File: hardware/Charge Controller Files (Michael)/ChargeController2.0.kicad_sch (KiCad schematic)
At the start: 90 parts, among them J1 GND_TEST_01x01_Pin, J10 SOL_TEST_01x01_Pin, J13 Conn-1x2, J14 Conn-1x2, J15 Conn-1x2, J17 SCL_MAS_01x01_Pin, J18 SDA_MAS_01x01_Pin, J19 SYS-1x2, J2 SP_01x02_Pin, J3 BATT_TEST_01x01_Pin, J4 3.3V_PULLUP_01x02_Pin, J5 BATT_01x02_Pin, J6 Conn-1x2, J7 Conn-1x2, J8 Conn-1x2, J9 SYS_TEST_01x01_Pin, Q1 SI2318DS-T1-E3, Q10 SI2318DS-T1-E3, Q11 SI2318DS-T1-E3, Q12 SI2318DS-T1-E3, Q2 SI2318DS-T1-E3, Q3 SI2318DS-T1-E3, Q4 SI2318DS-T1-E3, Q5 AONS66614, Q6 AONS66614, Q7 AONS66614, Q8 AONS66614, Q9 SI2318DS-T1-E3, SW1 100SP1T1B1M1QEH, U1 BQ25756ERRVR

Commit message: Update ChargeController2.0.kicad_sch
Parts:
- Q5, Q6, Q7, Q8: Arrow Part Number (none) -> AONS66614; Arrow Price/Stock (none) -> https://www.arrow.com/en/products/aons66614/alpha-and-omega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

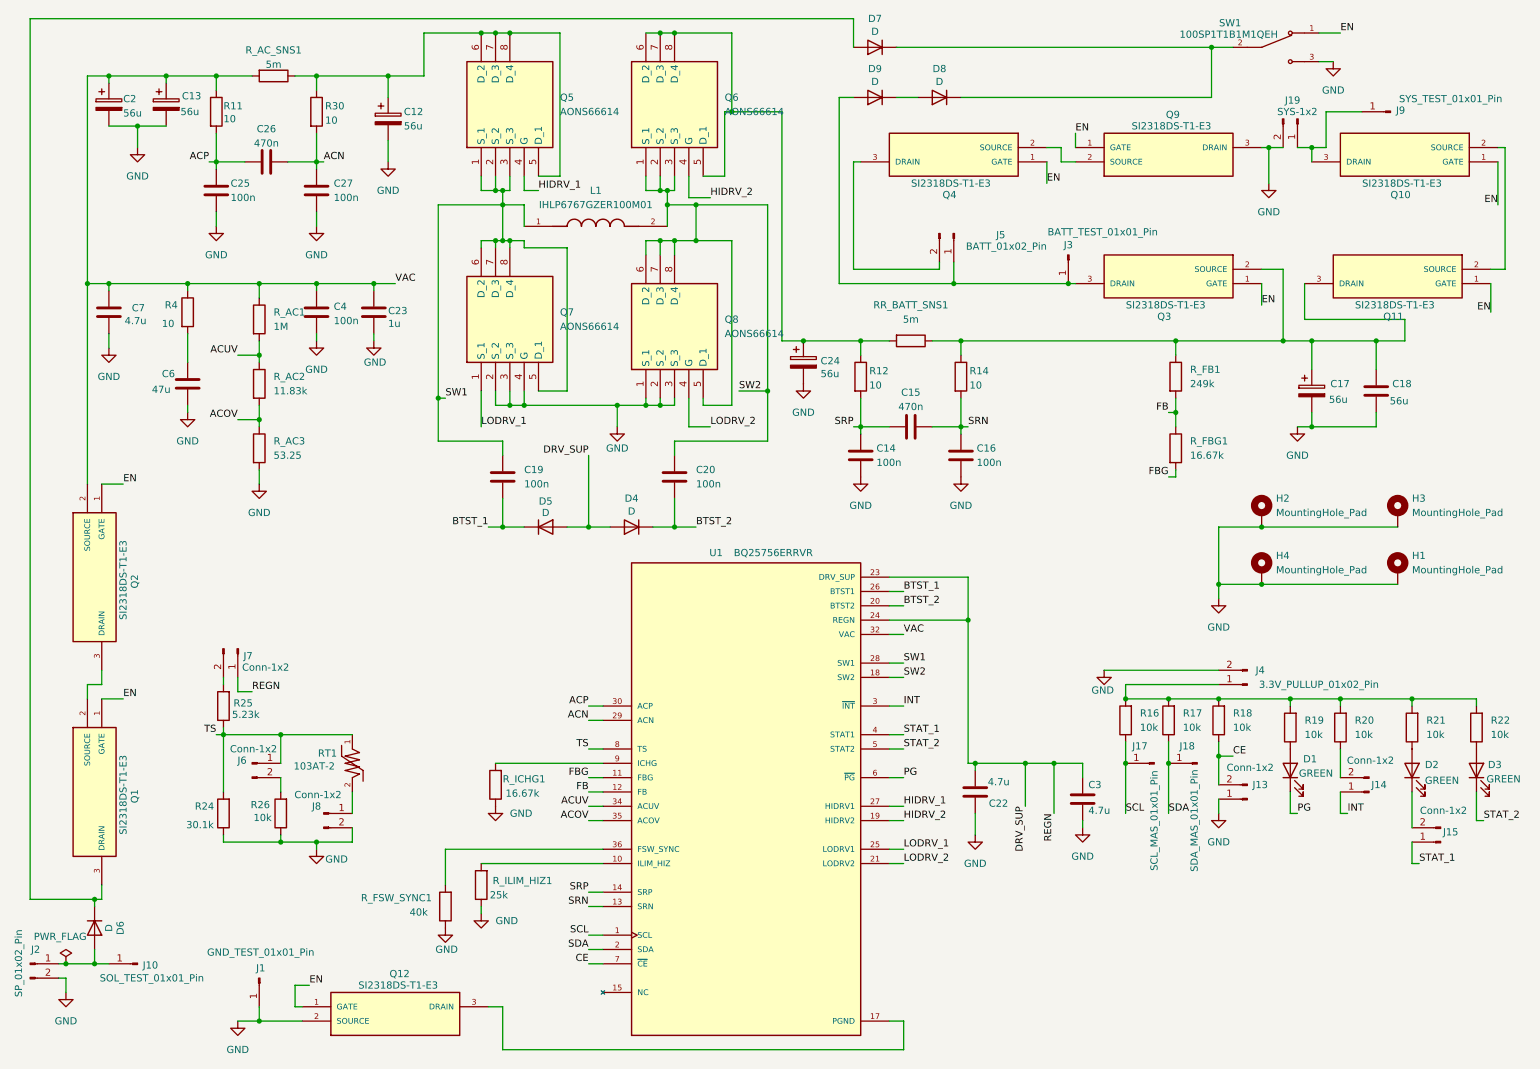
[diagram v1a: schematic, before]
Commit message: updated footprints
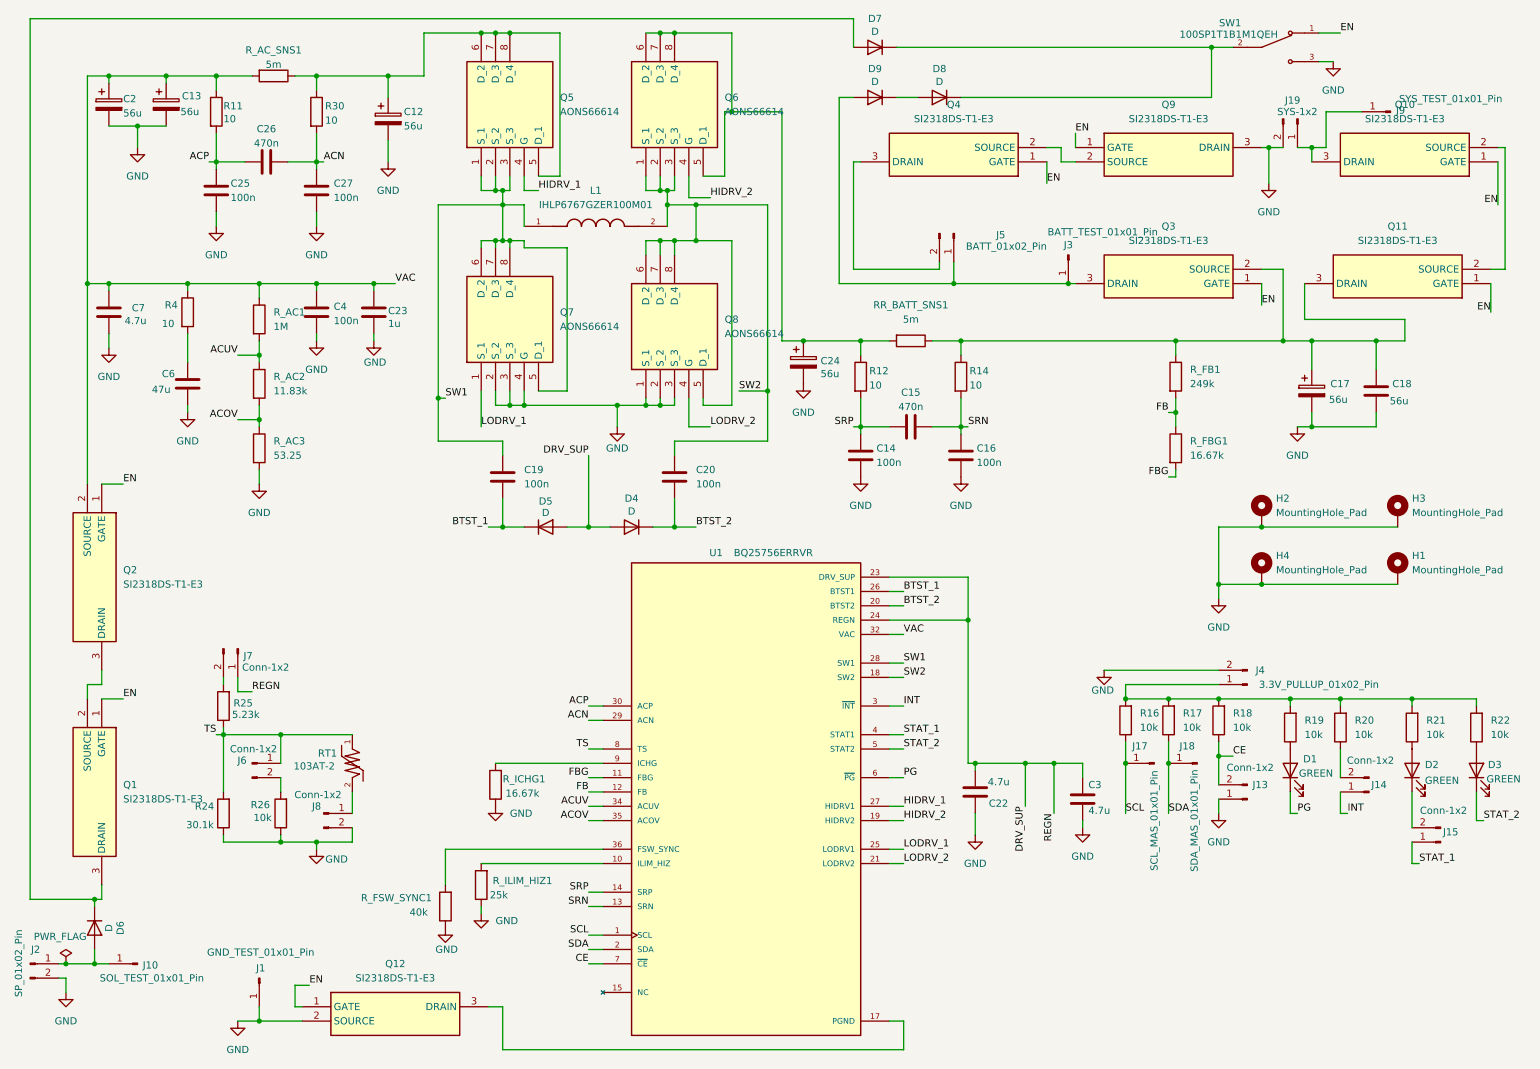
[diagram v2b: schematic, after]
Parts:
- Q1, Q2, Q3, Q4: ARROW_PART_NUMBER SI2318DS-T1-E3 -> (none); ARROW_PRICE-STOCK https://www.arrow.com/en/products/si2318ds-t1-e3/vishay -> (none); Availability In Stock -> (none); Check_prices https://www.snapeda.com/parts/SI2318DS-T1-E3/Vishay/view-pa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 -> (none); DESCRIPTION VISHAY - SI2318DS-T1-E3 - N CHANNEL MOSFET, 40V, 3.9A, TO-2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 -> (none); Description_1 N-CHANNEL 40-V (D-S) MOSFET | Siliconix / Vishay SI2318DS-T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 -> (none); HEIGHT 1.02mm -> (none); Height (none) -> 1.02; MANUFACTURER_NAME Vishay -> (none); MANUFACTURER_PART_NUMBER SI2318DS-T1-E3 -> (none); MF Vishay Siliconix -> (none); MOUSER_PART_NUMBER 781-SI2318DS-E3 -> (none); MOUSER_PRICE-STOCK https://www.mouser.co.uk/ProductDetail/Vishay-Semiconductor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 -> (none); MP SI2318DS-T1-E3 -> (none); Manufacturer_Name (none) -> Vishay; Manufacturer_Part_Number (none) -> SI2318DS-T1-E3; Mouser Part Number (none) -> 781-SI2318DS-E3; Mouser Price/Stock (none) -> https://www.mouser.co.uk/ProductDetail/Vishay-Semiconductor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; Package SOT-23-3 Vishay Siliconix -> (none); Price None -> (none); SnapEDA_Link https://www.snapeda.com/parts/SI2318DS-T1-E3/Vishay/view-pa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 -> (none)
- Q10, Q11, Q12, Q9: footprint bmsfootprints:SI2318DS-T1-E3 -> bmsfootprints:SOT95P237X102-3N; ARROW_PART_NUMBER SI2318DS-T1-E3 -> (none); ARROW_PRICE-STOCK https://www.arrow.com/en/products/si2318ds-t1-e3/vishay -> (none); Availability In Stock -> (none); Check_prices https://www.snapeda.com/parts/SI2318DS-T1-E3/Vishay/view-pa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 -> (none); DESCRIPTION VISHAY - SI2318DS-T1-E3 - N CHANNEL MOSFET, 40V, 3.9A, TO-2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 -> (none); Description_1 N-CHANNEL 40-V (D-S) MOSFET | Siliconix / Vishay SI2318DS-T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 -> (none); HEIGHT 1.02mm -> (none); Height (none) -> 1.02; MANUFACTURER_NAME Vishay -> (none); MANUFACTURER_PART_NUMBER SI2318DS-T1-E3 -> (none); MF Vishay Siliconix -> (none); MOUSER_PART_NUMBER 781-SI2318DS-E3 -> (none); MOUSER_PRICE-STOCK https://www.mouser.co.uk/ProductDetail/Vishay-Semiconductor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 -> (none); MP SI2318DS-T1-E3 -> (none); Manufacturer_Name (none) -> Vishay; Manufacturer_Part_Number (none) -> SI2318DS-T1-E3; Mouser Part Number (none) -> 781-SI2318DS-E3; Mouser Price/Stock (none) -> https://www.mouser.co.uk/ProductDetail/Vishay-Semiconductor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; Package SOT-23-3 Vishay Siliconix -> (none); Price None -> (none); SnapEDA_Link https://www.snapeda.com/parts/SI2318DS-T1-E3/Vishay/view-pa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 -> (none)

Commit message: Diode/Small Fixes
- Changed Inhibits MOSFETs to all be same footprint
- Changing diodes
   - Inhibits/Power Path -> SS24
   - Bootstrap -> BAT54
- LODRV_1 pin incorrectly placed
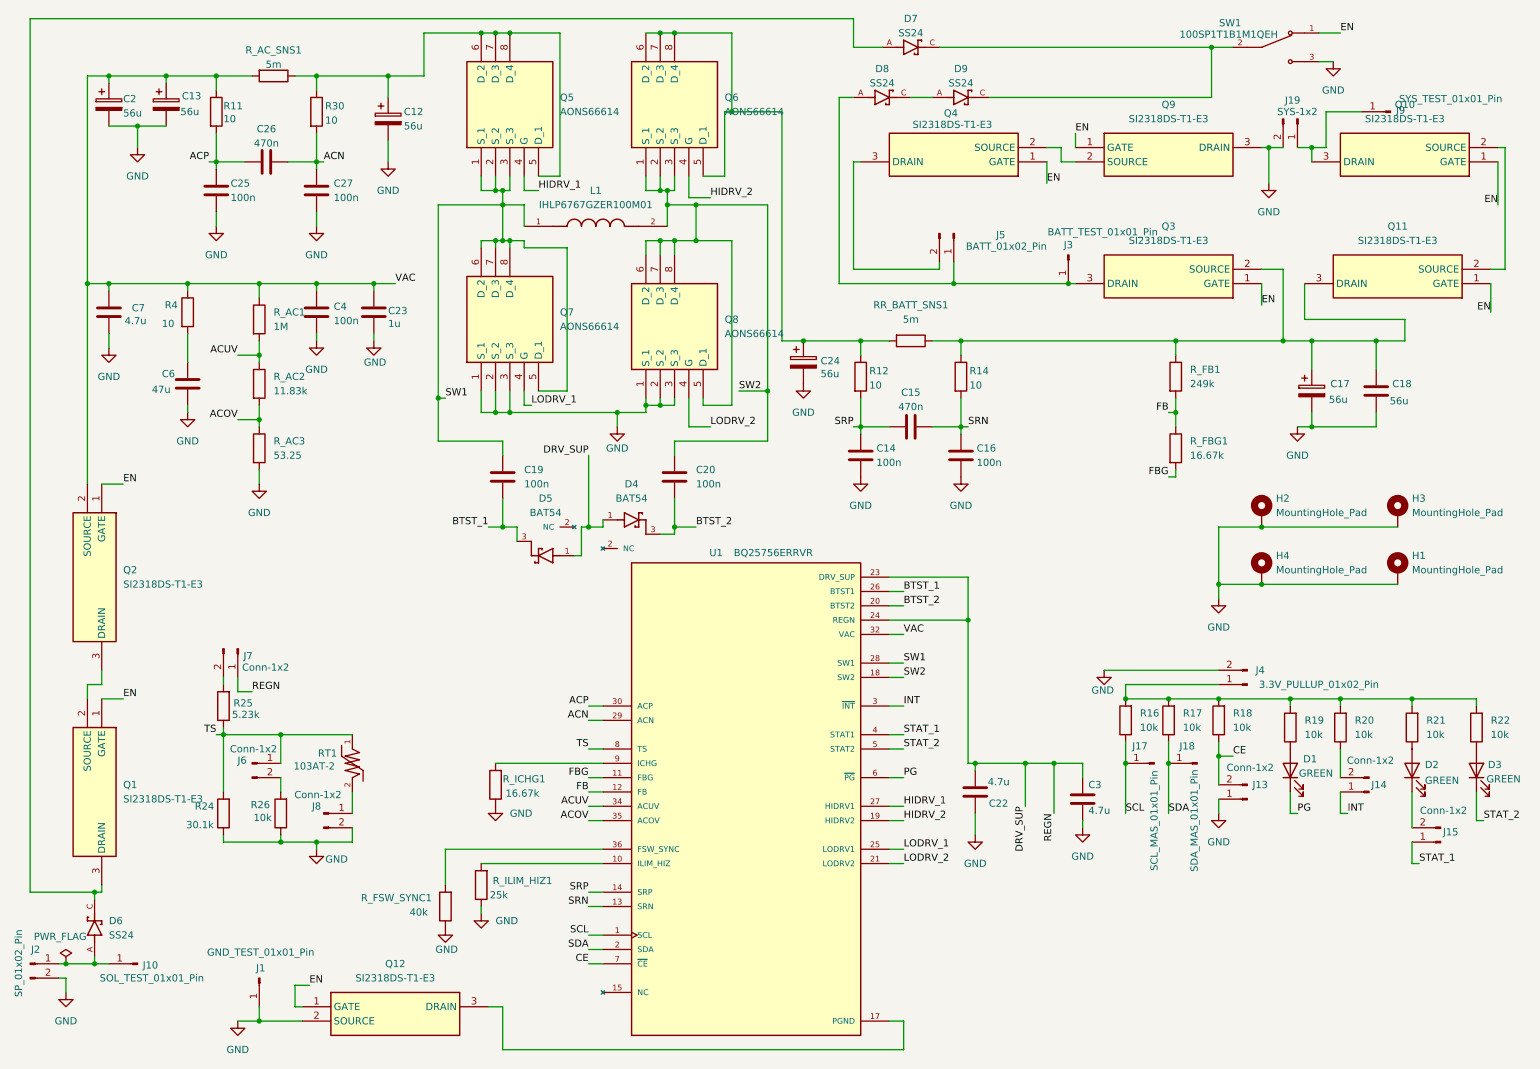
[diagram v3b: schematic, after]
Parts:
- removed D4, D5, D6, D7, D8, D9: D, bmsfootprints:DO-214AC, symbol Device:D
- added D4, D5: BAT54, bmsfootprints:BAT54, symbol BAT54:BAT54
- added D6, D7, D8, D9: SS24, bmsfootprints:SS24, symbol SS24:SS24
- J5: footprint Connector_PinHeader_2.54mm:PinHeader_1x01_P2.54mm_Vertical -> Connector_PinHeader_2.54mm:PinHeader_1x02_P2.54mm_Vertical
- Q10, Q11, Q12, Q9: footprint bmsfootprints:SOT95P237X102-3N -> bmsfootprints:SI2318DS-T1-E3
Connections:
- net BTST_1: now also D5.3
- net BTST_2: now also D4.3
- net DRV_SUP: now also D4.1, D5.1
- net GND: now also Q7.1 (S_1); no longer Q7.4 (G)
- net LODRV_1: now also Q7.4 (G); no longer Q7.1 (S_1)
- net at J3.1 (Pin_1), J5.1 (Pin_1), Q3.3 (DRAIN): now also D8.A
- net at SW1.2: now also D7.C, D9.C
- net at Q1.3 (DRAIN): now also D6.C, D7.A
- net at J10.1 (Pin_1), J2.1 (Pin_1): now also D6.A
- new net: D8.C, D9.A
